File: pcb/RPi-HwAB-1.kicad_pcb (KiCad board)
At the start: 6 copper layers, 65 x 56 mm, 130 parts, among them J1 GPIO, J2 Hirose_FH12-16S, J3 TC2030, U1 CAT24C256, U10 MT41K256M16TW-107:P TR, U11 INA230AIRGTR, U12 MCP9804T-E/MC, U13 INA230AIRGTR, U14 INA230AIRGTR, U2 TPSM82903, U3 TLV74312PDBVR, U4 TPSM82903, U5 AP3441SHE-7B, U6 AP3441SHE-7B, U7 XC7A100T-FGG484, U9 MX25L12835F, Y1 SiT9365AI-2B2-33E200.000000

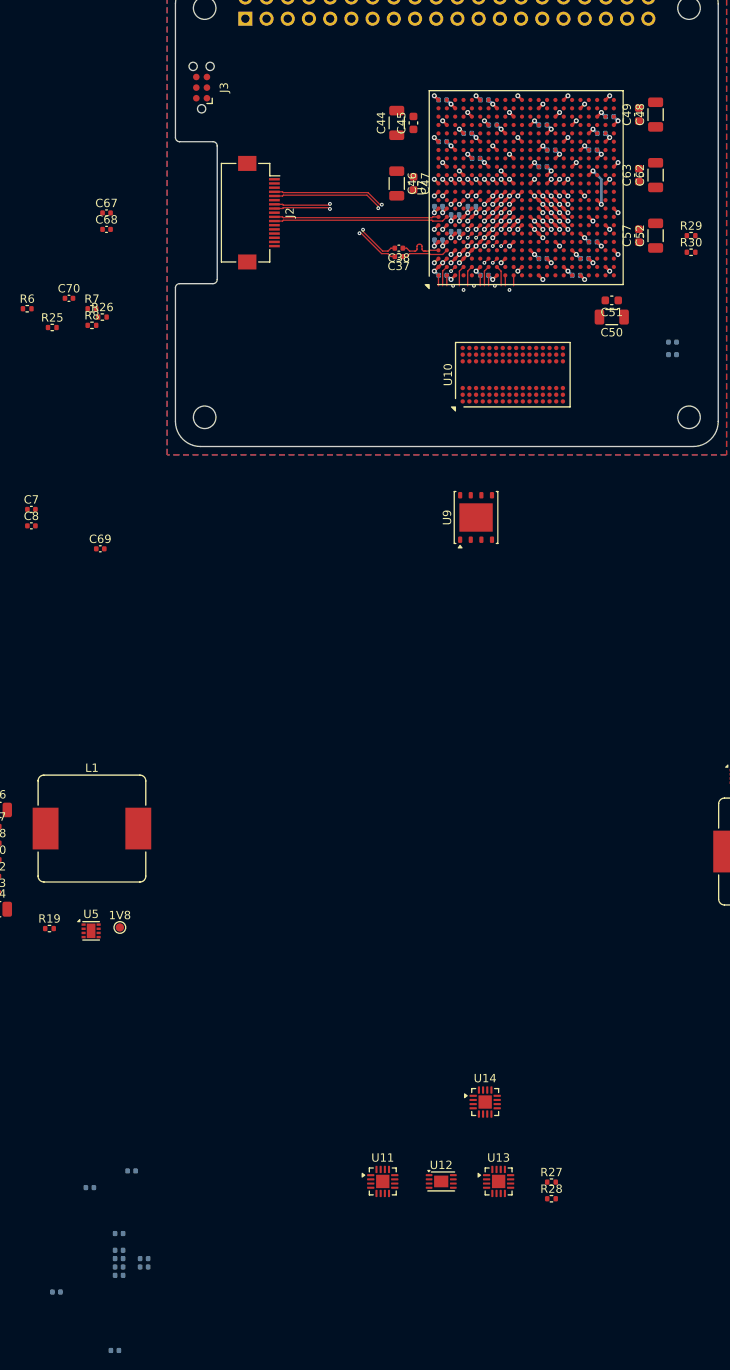
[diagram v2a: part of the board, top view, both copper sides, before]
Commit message: real ddr pinout done
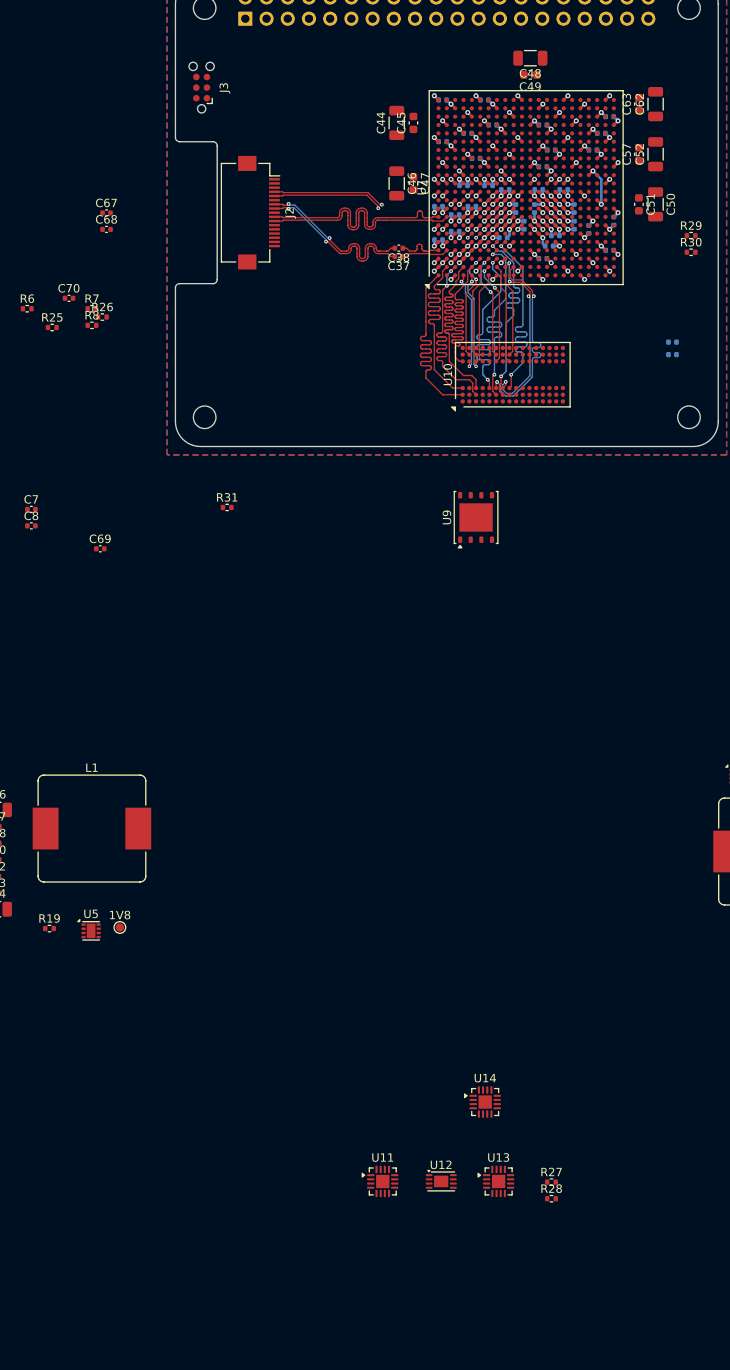
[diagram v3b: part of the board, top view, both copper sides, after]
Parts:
- added R31: 100 1%, Resistor_SMD:R_0402_1005Metric, F.Cu at (106.2, 107.3)
- moved C55 143.5 mm to (145.5, 74.8), turned to 0 degrees
- moved C56 142.0 mm to (147.8, 73.5), turned to 90 degrees
- moved C59 138.0 mm to (147.8, 71.5), turned to 90 degrees
- moved C58 136.9 mm to (134.5, 68.8)
- moved C64 135.9 mm to (137.5, 68.8), turned to 0 degrees
- moved C65 135.9 mm to (146.5, 69.2)
- moved C61 135.2 mm to (143.0, 71.5), turned to -90 degrees
- moved C66 133.5 mm to (140.8, 71.5), turned to 90 degrees
- moved C60 131.8 mm to (141.8, 73.5), turned to -90 degrees
- moved C53 129.4 mm to (139.5, 69.2)
- moved C54 127.2 mm to (143.5, 69.2)
- moved C31 20.2 mm to (152.0, 76.5)
- moved C48 16.4 mm to (142.5, 53.5), turned to 180 degrees
- moved C50 14.5 mm to (157.5, 71.0), turned to -90 degrees
- moved C49 13.8 mm to (142.5, 55.5), turned to 180 degrees
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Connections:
- C29 pad 1: Net-(U7E-IO_L12N_T1_MRCC_34) -> /FPGA/FPGA 3/DDR_SYSCLK_N
- C30 pad 1: Net-(U7E-IO_L12P_T1_MRCC_34) -> /FPGA/FPGA 3/DDR_SYSCLK_P
- R23 pad 2: Net-(U7E-IO_L12P_T1_MRCC_34) -> /FPGA/FPGA 3/DDR_SYSCLK_P
- R24 pad 1: Net-(U7E-IO_L12P_T1_MRCC_34) -> /FPGA/FPGA 3/DDR_SYSCLK_P
- U10 pad J7: /FPGA/FPGA 3/DDR_CKp -> /FPGA/FPGA 3/DDR_CK_P
- U10 pad K7: /FPGA/FPGA 3/DDR_CKn -> /FPGA/FPGA 3/DDR_CK_N
- U7 pad A1: /FPGA/FPGA 3/DQ1 -> /FPGA/FPGA 3/DQ13
- U7 pad AA1: /FPGA/FPGA 3/A13 -> /FPGA/FPGA 3/A4
- U7 pad AA18: unconnected-(U7B-IO_L17P_T2_A14_D30_14-PadAA18) -> /FPGA/FPGA 1/DDR_SYS_RESET
- U7 pad AA19: unconnected-(U7B-IO_L15P_T2_DQS_RDWR_B_14-PadAA19) -> /FPGA/FPGA 1/DDR_INIT_CALIB_COMPLETE
- U7 pad AA20: unconnected-(U7B-IO_L8P_T1_D11_14-PadAA20) -> /FPGA/FPGA 1/DDR_TG_COMPARE_ERROR
- U7 pad AA3: unconnected-(U7E-IO_L9N_T1_DQS_34-PadAA3) -> /FPGA/FPGA 3/DDR_BA2
- U7 pad AA4: unconnected-(U7E-IO_L11N_T1_SRCC_34-PadAA4) -> /FPGA/FPGA 3/DDR_CASn
- U7 pad AA5: unconnected-(U7E-IO_L10P_T1_34-PadAA5) -> /FPGA/FPGA 3/DDR_BA1
- U7 pad AA8: /FPGA/FPGA 3/DDR_RASn -> unconnected-(U7E-IO_L22P_T3_34-PadAA8)
- U7 pad AB1: /FPGA/FPGA 3/A14 -> /FPGA/FPGA 3/A3
- U7 pad AB2: unconnected-(U7E-IO_L8N_T1_34-PadAB2) -> /FPGA/FPGA 3/A1
- U7 pad AB3: unconnected-(U7E-IO_L8P_T1_34-PadAB3) -> /FPGA/FPGA 3/A2
- U7 pad AB5: unconnected-(U7E-IO_L10N_T1_34-PadAB5) -> /FPGA/FPGA 3/DDR_BA0
- U7 pad AB6: /FPGA/FPGA 3/DDR_BA1 -> unconnected-(U7E-IO_L20N_T3_34-PadAB6)
- U7 pad AB7: /FPGA/FPGA 3/DDR_BA0 -> unconnected-(U7E-IO_L20P_T3_34-PadAB7)
- U7 pad AB8: /FPGA/FPGA 3/DDR_CASn -> unconnected-(U7E-IO_L22N_T3_34-PadAB8)
- U7 pad B1: /FPGA/FPGA 3/DQ0 -> /FPGA/FPGA 3/DDR_UDM
- U7 pad B2: /FPGA/FPGA 3/DQ3 -> /FPGA/FPGA 3/DQ15
- U7 pad C2: /FPGA/FPGA 3/DQ2 -> /FPGA/FPGA 3/DQ11
- U7 pad D1: /FPGA/FPGA 3/DDR_LDQS_N -> /FPGA/FPGA 3/DDR_UDQS_N
- U7 pad D2: /FPGA/FPGA 3/DQ5 -> /FPGA/FPGA 3/DQ9
- U7 pad E1: /FPGA/FPGA 3/DDR_LDQS_P -> /FPGA/FPGA 3/DDR_UDQS_P
- U7 pad E2: /FPGA/FPGA 3/DQ4 -> /FPGA/FPGA 3/DQ12
- U7 pad F1: /FPGA/FPGA 3/DQ7 -> /FPGA/FPGA 3/DQ10
- U7 pad F3: /FPGA/FPGA 3/DDR_LDM -> /FPGA/FPGA 3/DQ14
- U7 pad G1: /FPGA/FPGA 3/DQ6 -> /FPGA/FPGA 3/DQ8
- U7 pad G2: /FPGA/FPGA 3/DQ11 -> /FPGA/FPGA 3/DQ1
- U7 pad G3: /FPGA/FPGA 3/DQ15 -> /FPGA/FPGA 3/DQ3
- U7 pad G4: unconnected-(U7F-IO_L12N_T1_MRCC_35-PadG4) -> /FPGA/FPGA 3/DDR_RESETn
- U7 pad H2: /FPGA/FPGA 3/DQ10 -> /FPGA/FPGA 3/DQ7
- U7 pad H3: /FPGA/FPGA 3/DQ14 -> /FPGA/FPGA 3/DQ0
- U7 pad H4: /FPGA/FPGA 3/DDR_UDM -> /FPGA/FPGA 3/DQ2
- U7 pad H5: /FPGA/FPGA 3/DQ13 -> /FPGA/FPGA 3/DQ6
- U7 pad J1: /FPGA/FPGA 3/DQ9 -> /FPGA/FPGA 3/DQ5
- U7 pad J2: /FPGA/FPGA 3/DDR_UDQS_N -> /FPGA/FPGA 3/DDR_LDQS_N
- U7 pad J5: /FPGA/FPGA 3/DQ12 -> /FPGA/FPGA 3/DQ4
- U7 pad K1: /FPGA/FPGA 3/DQ8 -> /FPGA/FPGA 3/DDR_LDM
- U7 pad K2: /FPGA/FPGA 3/DDR_UDQS_P -> /FPGA/FPGA 3/DDR_LDQS_P
- U7 pad R2: /FPGA/FPGA 3/A6 -> /FPGA/FPGA 3/DDR_CK_N
- U7 pad R3: /FPGA/FPGA 3/A5 -> /FPGA/FPGA 3/DDR_CK_P
- U7 pad R4: unconnected-(U7E-IO_L13P_T2_MRCC_34-PadR4) -> /FPGA/FPGA 3/DDR_SYSCLK_P
- U7 pad T1: /FPGA/FPGA 3/A1 -> /FPGA/FPGA 3/A14
- U7 pad T3: /FPGA/FPGA 3/A0 -> unconnected-(U7E-IO_0_34-PadT3)
- U7 pad T4: unconnected-(U7E-IO_L13N_T2_MRCC_34-PadT4) -> /FPGA/FPGA 3/DDR_SYSCLK_N
- U7 pad T5: unconnected-(U7E-IO_L14P_T2_SRCC_34-PadT5) -> /FPGA/FPGA 3/DDR_CLK_REF_P
- U7 pad U1: /FPGA/FPGA 3/A2 -> /FPGA/FPGA 3/A13
- U7 pad U2: /FPGA/FPGA 3/A3 -> /FPGA/FPGA 3/A12
- U7 pad U3: /FPGA/FPGA 3/A11 -> /FPGA/FPGA 3/A6
- U7 pad U5: unconnected-(U7E-IO_L14N_T2_SRCC_34-PadU5) -> /FPGA/FPGA 3/DDR_CLK_REF_N
- U7 pad U7: /FPGA/FPGA 3/DDR_CKn -> unconnected-(U7E-IO_25_34-PadU7)
- U7 pad V2: /FPGA/FPGA 3/A4 -> /FPGA/FPGA 3/A11
- U7 pad V3: /FPGA/FPGA 3/A12 -> /FPGA/FPGA 3/A5
- U7 pad V4: Net-(U7E-IO_L12P_T1_MRCC_34) -> /FPGA/FPGA 3/DDR_WEn
- U7 pad V8: /FPGA/FPGA 3/DDR_CSn -> unconnected-(U7E-IO_L21N_T3_DQS_34-PadV8)
- U7 pad V9: /FPGA/FPGA 3/DDR_BA2 -> unconnected-(U7E-IO_L21P_T3_DQS_34-PadV9)
- U7 pad W1: /FPGA/FPGA 3/A9 -> /FPGA/FPGA 3/A8
- U7 pad W2: /FPGA/FPGA 3/A7 -> /FPGA/FPGA 3/A10
- U7 pad W4: Net-(U7E-IO_L12N_T1_MRCC_34) -> /FPGA/FPGA 3/DDR_CSn
- U7 pad W5: unconnected-(U7E-IO_L15N_T2_DQS_34-PadW5) -> /FPGA/FPGA 3/DDR_ODT
- U7 pad W6: unconnected-(U7E-IO_L15P_T2_DQS_34-PadW6) -> /FPGA/FPGA 3/DDR_CKE
- U7 pad W7: /FPGA/FPGA 3/DDR_RESETn -> unconnected-(U7E-IO_L19N_T3_VREF_34-PadW7)
- U7 pad W9: /FPGA/FPGA 3/DDR_CKE -> unconnected-(U7E-IO_L24P_T3_34-PadW9)
- U7 pad Y1: /FPGA/FPGA 3/A10 -> /FPGA/FPGA 3/A7
- U7 pad Y2: /FPGA/FPGA 3/A8 -> /FPGA/FPGA 3/A9
- U7 pad Y3: unconnected-(U7E-IO_L9P_T1_DQS_34-PadY3) -> /FPGA/FPGA 3/A0
- U7 pad Y4: unconnected-(U7E-IO_L11P_T1_SRCC_34-PadY4) -> /FPGA/FPGA 3/DDR_RASn
- U7 pad Y7: /FPGA/FPGA 3/DDR_ODT -> unconnected-(U7E-IO_L23N_T3_34-PadY7)
- U7 pad Y8: /FPGA/FPGA 3/DDR_WEn -> unconnected-(U7E-IO_L23P_T3_34-PadY8)
- U7 pad Y9: /FPGA/FPGA 3/DDR_CKp -> unconnected-(U7E-IO_L24N_T3_34-PadY9)
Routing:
- net /FPGA/FPGA 3/DQ9: track 1.25 -> 26.7 mm
- net /FPGA/FPGA 3/DDR_LDQS_P: track 0.00 -> 25.3 mm, vias 0 -> 2
- net /FPGA/FPGA 3/DQ6: track 1.25 -> 25.3 mm, vias 0 -> 2
- net /FPGA/FPGA 3/DQ0: track 1.25 -> 25.2 mm, vias 0 -> 2
- net /FPGA/FPGA 3/DQ4: track 2.46 -> 25.3 mm, vias 0 -> 2
- net /FPGA/FPGA 3/DQ11: track 2.46 -> 25.2 mm, vias 0 -> 2
- net /FPGA/FPGA 3/DQ15: track 3.97 -> 26.7 mm, vias 2 -> 0
- net /FPGA/FPGA 3/DDR_LDQS_N: track 0.00 -> 22.5 mm, vias 0 -> 4
- net /FPGA/FPGA 3/DQ2: track 2.97 -> 25.3 mm
- net /FPGA/FPGA 3/DQ12: track 6.37 -> 26.7 mm, vias 2 -> 0
- net /FPGA/FPGA 3/DQ13: track 7.41 -> 26.7 mm, vias 2 -> 0
- net /FPGA/FPGA 3/DDR_UDQS_N: track 0.00 -> 12.2 mm, vias 0 -> 2
- net /FPGA/FPGA 3/DDR_UDQS_P: track 0.00 -> 12.1 mm, vias 0 -> 2
- net /FPGA/FPGA 3/DQ1: track 1.25 -> 12.4 mm, vias 0 -> 2
- net /FPGA/FPGA 3/DQ7: track 1.25 -> 11.9 mm
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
